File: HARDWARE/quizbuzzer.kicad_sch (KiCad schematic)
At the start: 27 parts, among them J1 Controls, J10 Reciver 5, J11 Reciver 6, J12 Reciver 7, J13 Reciver 8, J14 Reciver 10, J2 MP3out, J25 Conn_02x12_Odd_Even, J26 I2C, J3 I2C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

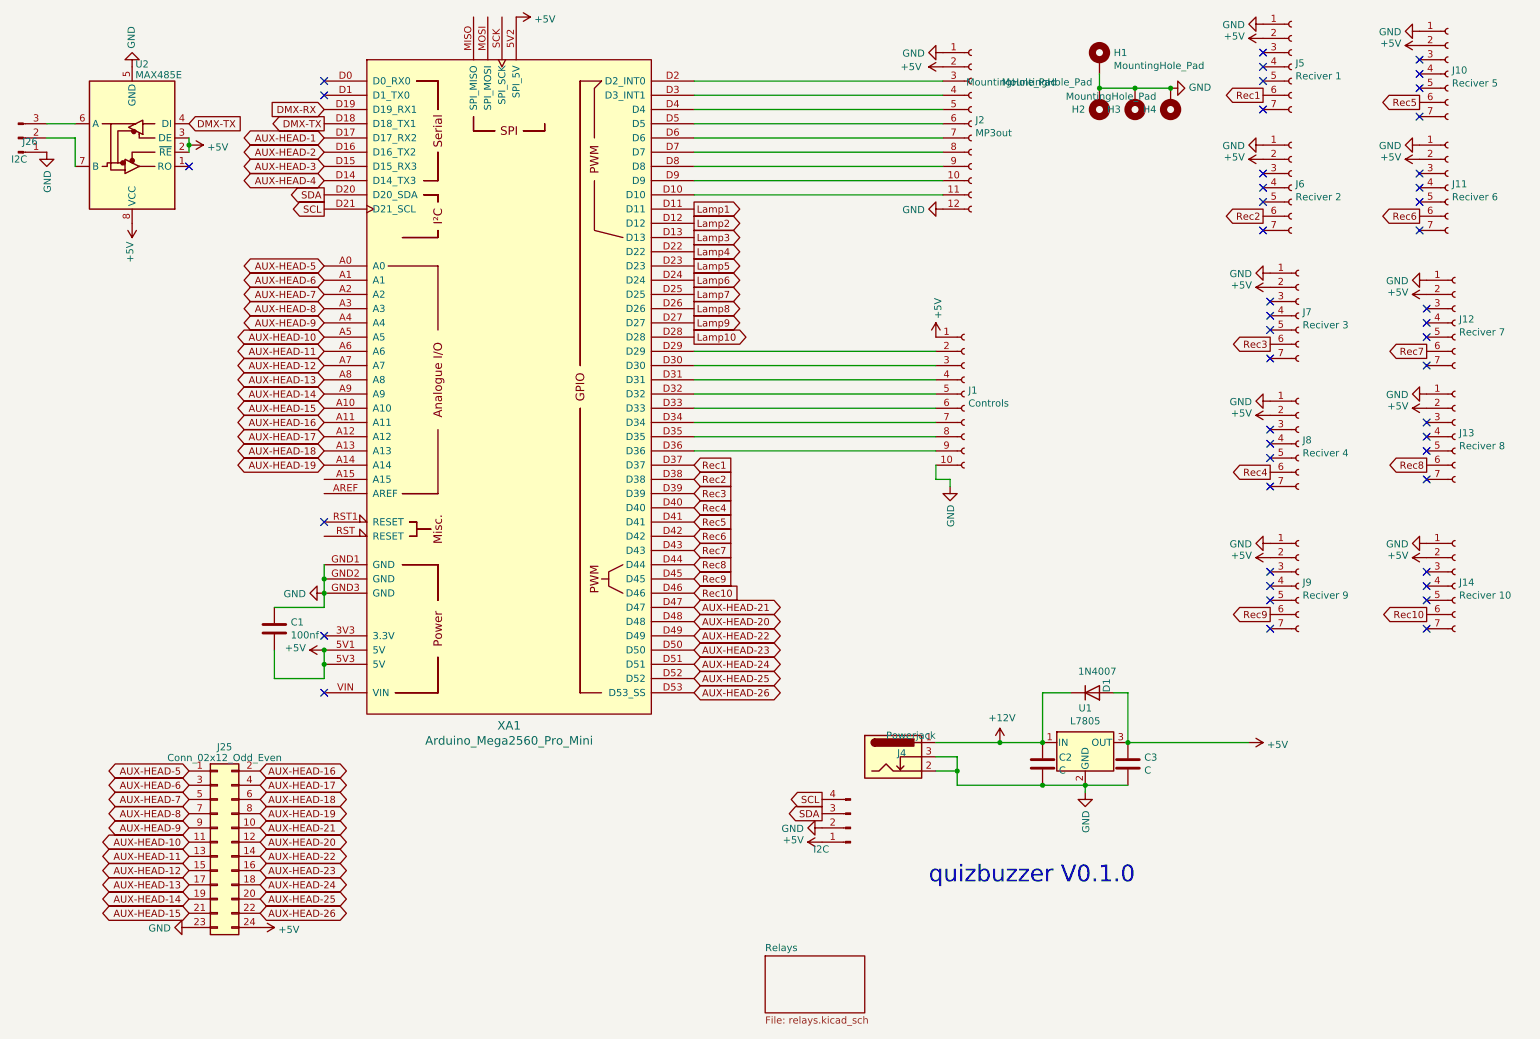
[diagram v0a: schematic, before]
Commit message: Updated schematic for portB, updated code with new variables, stuck at seetting pin mode in loop.
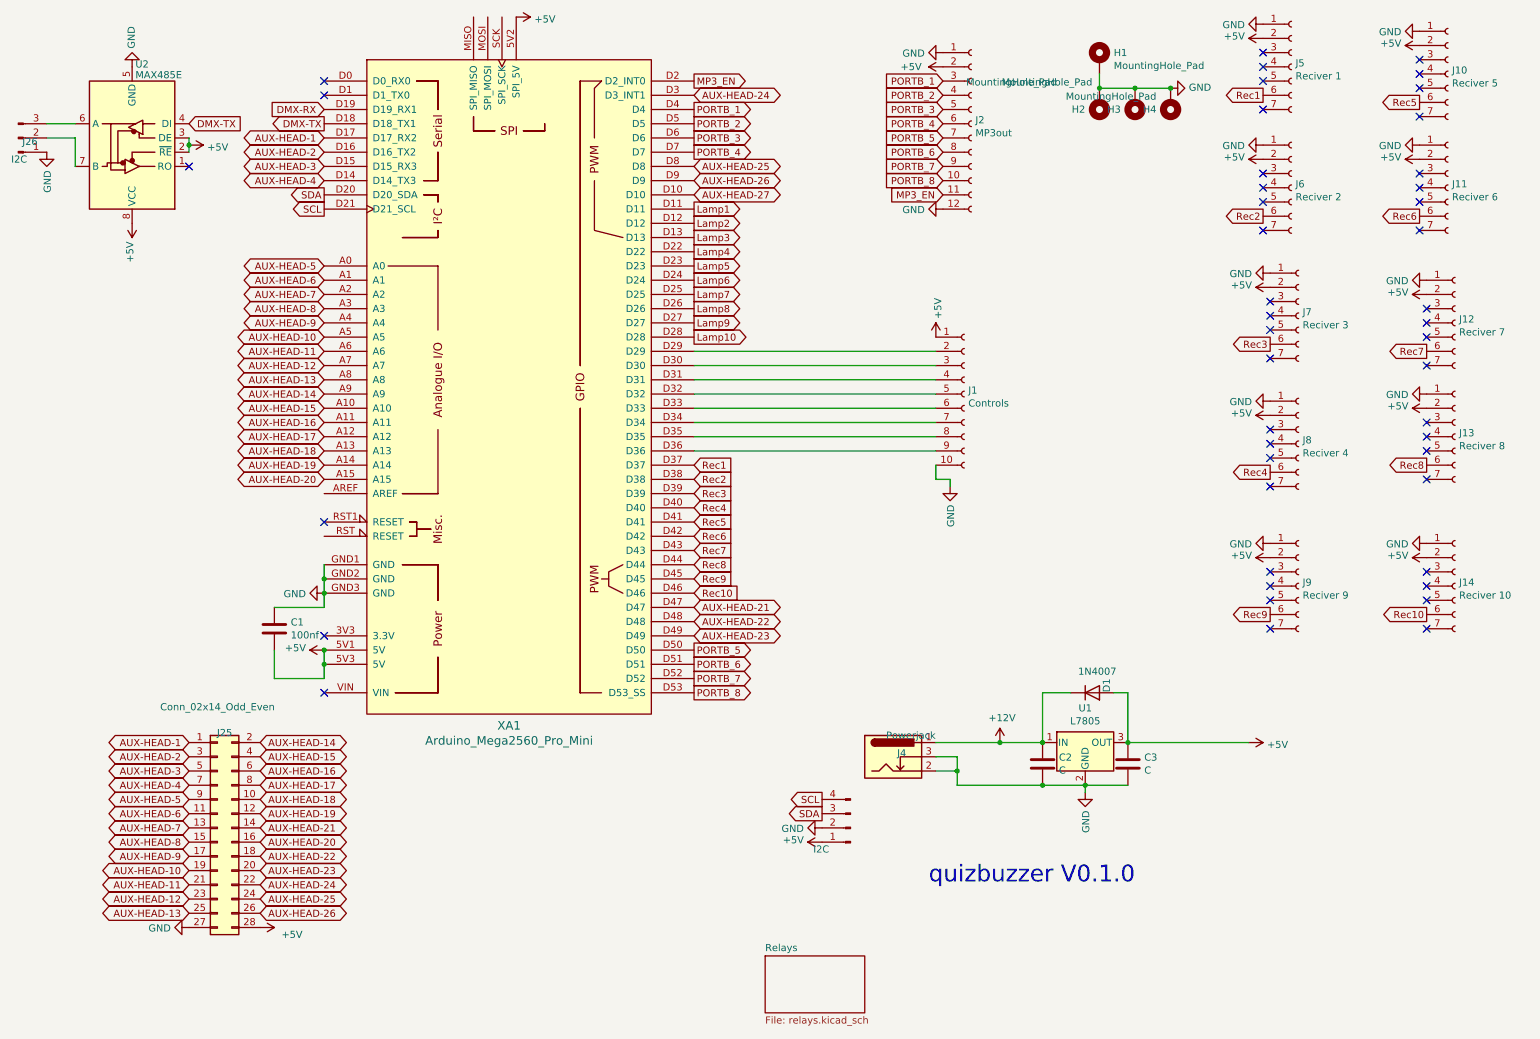
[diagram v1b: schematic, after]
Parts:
- J25: value Conn_02x12_Odd_Even -> Conn_02x14_Odd_Even; footprint Connector_PinHeader_2.54mm:PinHeader_2x12_P2.54mm_Vertical -> Connector_PinHeader_2.54mm:PinHeader_2x14_P2.54mm_Vertical; symbol Connector_Generic:Conn_02x12_Odd_Even -> Connector_Generic:Conn_02x14_Odd_Even
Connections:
- net +5V: now also J25.28 (Pin_28); no longer J25.24 (Pin_24)
- net AUX-HEAD-1: now also J25.1 (Pin_1)
- net AUX-HEAD-10: now also J25.19 (Pin_19); no longer J25.11 (Pin_11)
- net AUX-HEAD-11: now also J25.21 (Pin_21); no longer J25.13 (Pin_13)
- net AUX-HEAD-12: now also J25.23 (Pin_23); no longer J25.15 (Pin_15)
- net AUX-HEAD-13: now also J25.25 (Pin_25); no longer J25.17 (Pin_17)
- net AUX-HEAD-14: now also J25.2 (Pin_2); no longer J25.19 (Pin_19)
- net AUX-HEAD-15: now also J25.4 (Pin_4); no longer J25.21 (Pin_21)
- net AUX-HEAD-16: now also J25.6 (Pin_6); no longer J25.2 (Pin_2)
- net AUX-HEAD-17: now also J25.8 (Pin_8); no longer J25.4 (Pin_4)
- net AUX-HEAD-18: now also J25.10 (Pin_10); no longer J25.6 (Pin_6)
- net AUX-HEAD-19: now also J25.12 (Pin_12); no longer J25.8 (Pin_8)
- net AUX-HEAD-2: now also J25.3 (Pin_3)
- net AUX-HEAD-20: now also J25.16 (Pin_16), XA1.A15; no longer J25.12 (Pin_12), XA1.D48
- net AUX-HEAD-21: now also J25.14 (Pin_14); no longer J25.10 (Pin_10)
- net AUX-HEAD-22: now also J25.18 (Pin_18), XA1.D48; no longer J25.14 (Pin_14), XA1.D49
- net AUX-HEAD-23: now also J25.20 (Pin_20), XA1.D49; no longer J25.16 (Pin_16), XA1.D50
- net AUX-HEAD-24: now also J25.22 (Pin_22), XA1.D3 (D3_INT1); no longer J25.18 (Pin_18), XA1.D51
- net AUX-HEAD-25: now also J25.24 (Pin_24), XA1.D8; no longer J25.20 (Pin_20), XA1.D52
- net AUX-HEAD-26: now also J25.26 (Pin_26), XA1.D9; no longer J25.22 (Pin_22), XA1.D53 (D53_SS)
- net AUX-HEAD-3: now also J25.5 (Pin_5)
- net AUX-HEAD-4: now also J25.7 (Pin_7)
- net AUX-HEAD-5: now also J25.9 (Pin_9); no longer J25.1 (Pin_1)
- net AUX-HEAD-6: now also J25.11 (Pin_11); no longer J25.3 (Pin_3)
- net AUX-HEAD-7: now also J25.13 (Pin_13); no longer J25.5 (Pin_5)
- net AUX-HEAD-8: now also J25.15 (Pin_15); no longer J25.7 (Pin_7)
- net AUX-HEAD-9: now also J25.17 (Pin_17); no longer J25.9 (Pin_9)
- net GND: now also J25.27 (Pin_27); no longer J25.23 (Pin_23)
- net PORTB_8: now reaches J2.10 (Pin_10)
- net PORTB_8: now also XA1.D53 (D53_SS); no longer XA1.D9
- net AUX-HEAD-27: now reaches XA1.D10
- net AUX-HEAD-27: no longer J2.11 (Pin_11)
- net MP3_EN: now reaches XA1.D2 (D2_INT0)
- net MP3_EN: now also J2.11 (Pin_11); no longer J2.3 (Pin_3)
- net PORTB_2: now reaches J2.4 (Pin_4)
- net PORTB_2: now also XA1.D5; no longer XA1.D3 (D3_INT1)
- net PORTB_1: now reaches XA1.D4
- net PORTB_1: now also J2.3 (Pin_3); no longer J2.5 (Pin_5)
- net PORTB_4: now reaches J2.6 (Pin_6)
- net PORTB_4: now also XA1.D7; no longer XA1.D5
- net PORTB_3: now reaches XA1.D6
- net PORTB_3: now also J2.5 (Pin_5); no longer J2.7 (Pin_7)
- net PORTB_6: now reaches J2.8 (Pin_8)
- net PORTB_6: now also XA1.D51; no longer XA1.D7
- net PORTB_7: now reaches J2.9 (Pin_9)
- net PORTB_7: now also XA1.D52; no longer XA1.D8
- new net PORTB_5: J2.7 (Pin_7), XA1.D50

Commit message: FIXLAYER
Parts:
- J26: value I2C -> DMX
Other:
- note removed: "quizbuzzer V0.1.0"
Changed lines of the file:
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@@
     (stroke (width 0) (type default))
-  )
-  (text "quizbuzzer V0.1.0" (at 179.07 171.45 0)
-    (effects (font (size 2.9972 2.9972)) (justify left bottom))
   )
   (global_label "Lamp2" (shape output) (at 137.16 53.34 0)
@@
       (effects (font (size 1.27 1.27)) (justify left))
     )
-    (property "Value" "I2C" (at 15.24 41.91 0)
-      (effects (font (size 1.27 1.27)) (justify left))
-    )
+    (property "Value" "DMX" (at 15.24 41.91 0)
+      (effects (font (size 1.27 1.27)) (justify left))
+    )

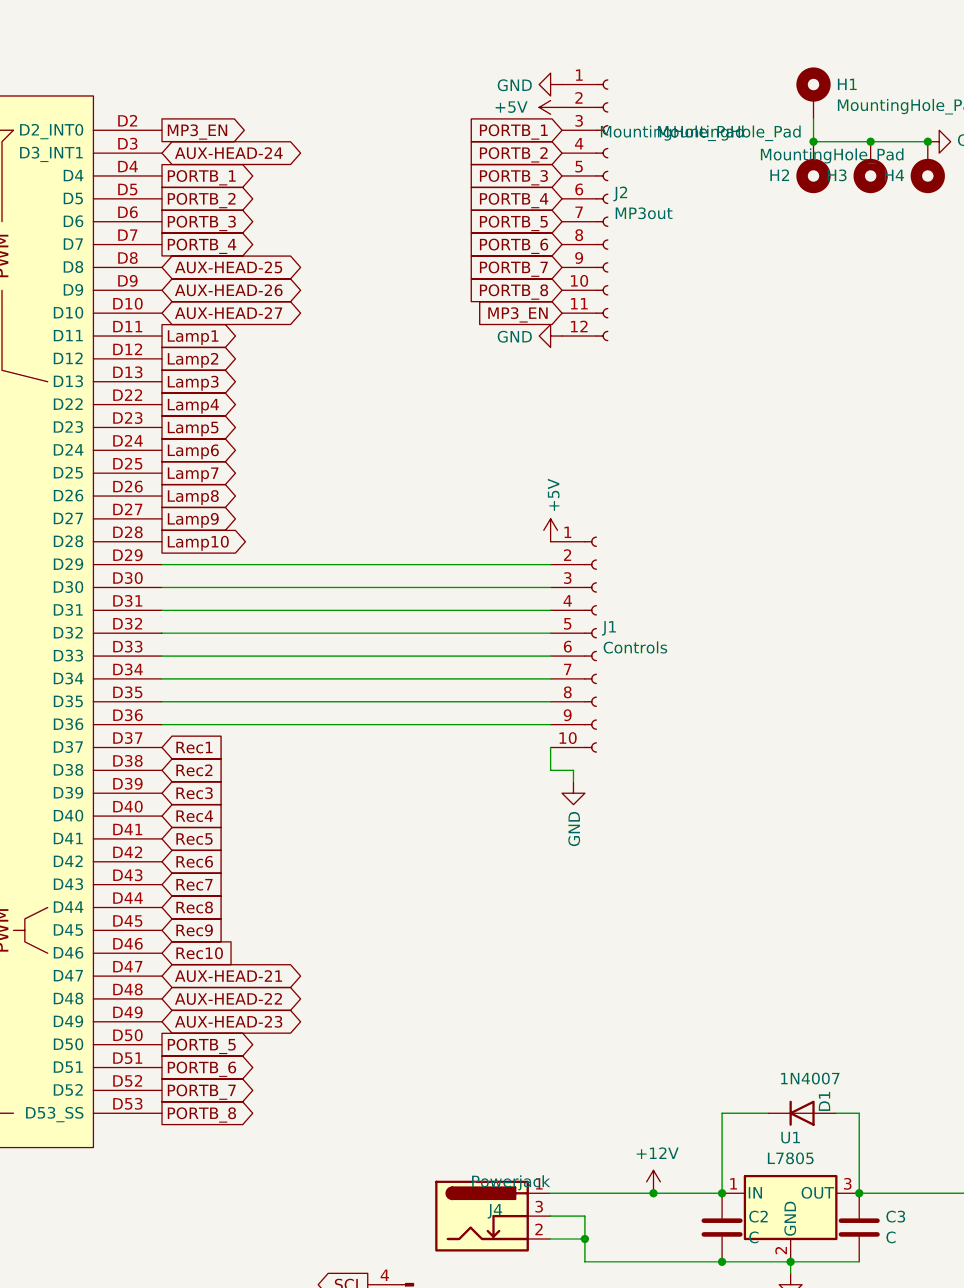
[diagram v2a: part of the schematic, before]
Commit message: Port Sort + 10 to 8 channel
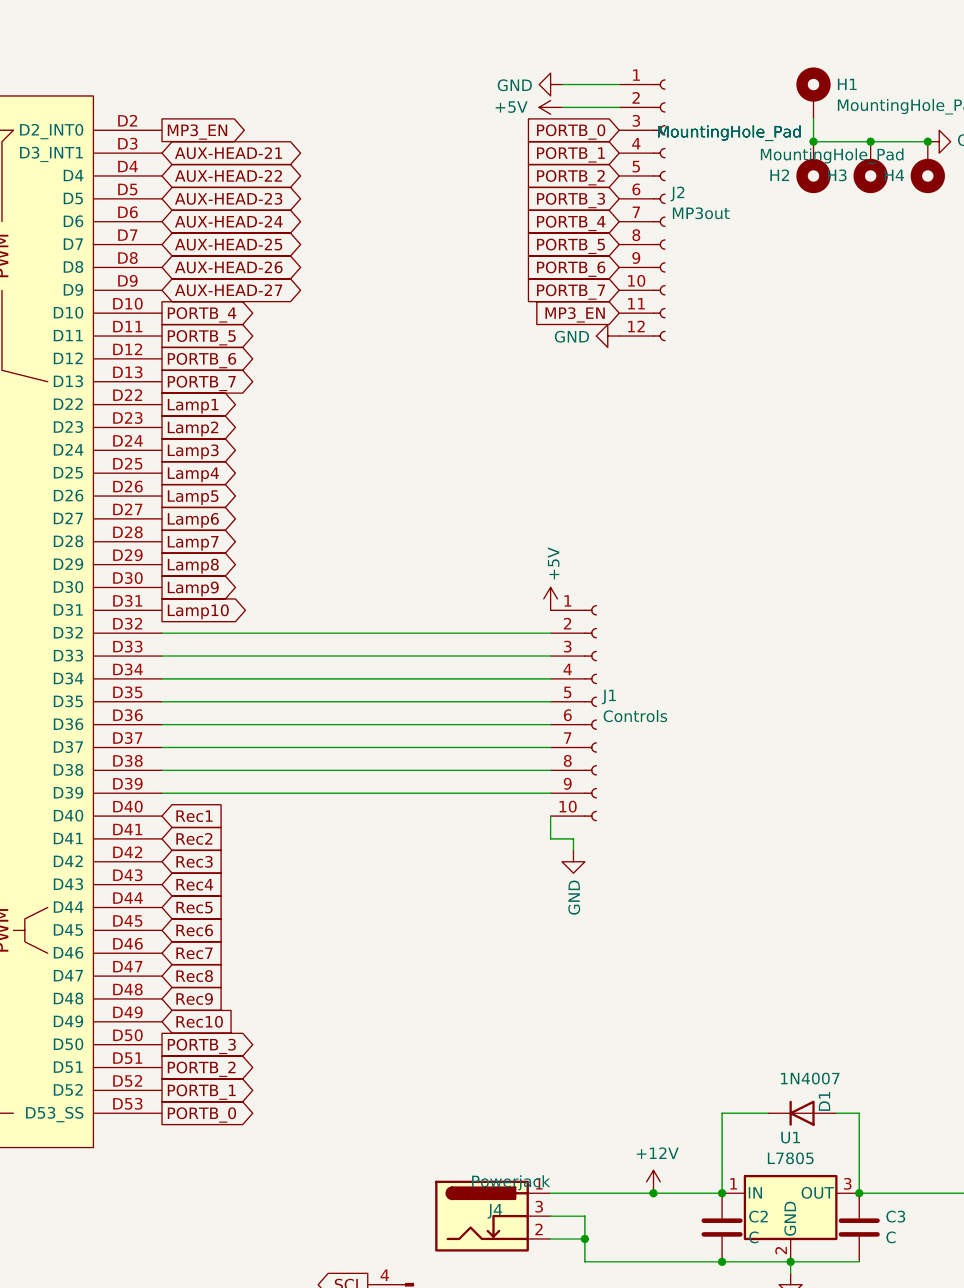
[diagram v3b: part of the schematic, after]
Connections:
- net AUX-HEAD-21: now also XA1.D3 (D3_INT1); no longer XA1.D47
- net AUX-HEAD-22: now also XA1.D4; no longer XA1.D48
- net AUX-HEAD-23: now also XA1.D5; no longer XA1.D49
- net AUX-HEAD-24: now also XA1.D6; no longer XA1.D3 (D3_INT1)
- net AUX-HEAD-25: now also XA1.D7; no longer XA1.D8
- net AUX-HEAD-26: now also XA1.D8; no longer XA1.D9
- net AUX-HEAD-27: now also XA1.D9; no longer XA1.D10
- net Lamp1: now also XA1.D22; no longer XA1.D11
- net Lamp10: now also XA1.D31; no longer XA1.D28
- net Lamp2: now also XA1.D23; no longer XA1.D12
- net Lamp3: now also XA1.D24; no longer XA1.D13
- net Lamp4: now also XA1.D25; no longer XA1.D22
- net Lamp5: now also XA1.D26; no longer XA1.D23
- net Lamp6: now also XA1.D27; no longer XA1.D24
- net Lamp7: now also XA1.D28; no longer XA1.D25
- net Lamp8: now also XA1.D29; no longer XA1.D26
- net Lamp9: now also XA1.D30; no longer XA1.D27
- net PORTB_1: now also J2.4 (Pin_4), XA1.D52; no longer J2.3 (Pin_3), XA1.D4
- net PORTB_2: now also J2.5 (Pin_5), XA1.D51; no longer J2.4 (Pin_4), XA1.D5
- net PORTB_3: now also J2.6 (Pin_6), XA1.D50; no longer J2.5 (Pin_5), XA1.D6
- net PORTB_4: now also J2.7 (Pin_7), XA1.D10; no longer J2.6 (Pin_6), XA1.D7
- net PORTB_5: now also J2.8 (Pin_8), XA1.D11; no longer J2.7 (Pin_7), XA1.D50
- net PORTB_6: now also J2.9 (Pin_9), XA1.D12; no longer J2.8 (Pin_8), XA1.D51
- net PORTB_7: now also J2.10 (Pin_10), XA1.D13; no longer J2.9 (Pin_9), XA1.D52
- net Rec1: now also XA1.D40; no longer XA1.D37
- net Rec10: now also XA1.D49; no longer XA1.D46
- net Rec2: now also XA1.D41; no longer XA1.D38
- net Rec3: now also XA1.D42; no longer XA1.D39
- net Rec4: now also XA1.D43; no longer XA1.D40
- net Rec5: now also XA1.D44; no longer XA1.D41
- net Rec6: now also XA1.D45; no longer XA1.D42
- net Rec7: now also XA1.D46; no longer XA1.D43
- net Rec8: now also XA1.D47; no longer XA1.D44
- net Rec9: now also XA1.D48; no longer XA1.D45
- net at J1.2 (Pin_2): now also XA1.D32; no longer XA1.D29
- net at J1.3 (Pin_3): now also XA1.D33; no longer XA1.D30
- net at J1.4 (Pin_4): now also XA1.D34; no longer XA1.D31
- net at J1.5 (Pin_5): now also XA1.D35; no longer XA1.D32
- net at J1.6 (Pin_6): now also XA1.D36; no longer XA1.D33
- net at J1.7 (Pin_7): now also XA1.D37; no longer XA1.D34
- net at J1.8 (Pin_8): now also XA1.D38; no longer XA1.D35
- net at J1.9 (Pin_9): now also XA1.D39; no longer XA1.D36
- net PORTB_8 renamed PORTB_0
- net PORTB_0: now also J2.3 (Pin_3); no longer J2.10 (Pin_10)
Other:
- moved on the sheet: J1, J2

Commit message: Code sanitisation part 1
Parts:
- removed J14: Reciver 10, Connector_PinSocket_2.54mm:PinSocket_1x07_P2.54mm_Vertical, symbol quizbuzzer-rescue:Conn_01x07_Female-Connector
- removed J9: Reciver 9, Connector_PinSocket_2.54mm:PinSocket_1x07_P2.54mm_Vertical, symbol quizbuzzer-rescue:Conn_01x07_Female-Connector
- J25: value Conn_02x14_Odd_Even -> Conn_02x09_Odd_Even; footprint Connector_PinHeader_2.54mm:PinHeader_2x14_P2.54mm_Vertical -> Connector_PinHeader_2.54mm:PinHeader_2x09_P2.54mm_Vertical; symbol Connector_Generic:Conn_02x14_Odd_Even -> Connector_Generic:Conn_02x09_Odd_Even
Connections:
- net AUX-HEAD-20 is gone; now on net AUX-HEAD-16: J25.16 (Pin_16), XA1.A15
- net Lamp10 is gone; now on an unnamed net: XA1.D31
- net Lamp9 is gone; now on an unnamed net: XA1.D30
- net Rec10 is gone; now on net Rec8: XA1.D49
- net Rec9 is gone; now on net Rec7: XA1.D48
- net +5V: now also J25.18 (Pin_18); no longer J25.28 (Pin_28)
- net AUX-HEAD-1: now also XA1.A0; no longer XA1.D17 (D17_RX2)
- net AUX-HEAD-10: now also J25.4 (Pin_4), XA1.A9; no longer J25.19 (Pin_19), XA1.A5
- net AUX-HEAD-11: now also J25.6 (Pin_6), XA1.A10; no longer J25.21 (Pin_21), XA1.A6
- net AUX-HEAD-12: now also J25.8 (Pin_8), XA1.A11; no longer J25.23 (Pin_23), XA1.A7
- net AUX-HEAD-13: now also J25.10 (Pin_10), XA1.A12; no longer J25.25 (Pin_25), XA1.A8
- net AUX-HEAD-14: now also J25.12 (Pin_12), XA1.A13; no longer J25.2 (Pin_2), XA1.A9
- net AUX-HEAD-15: now also J25.14 (Pin_14), XA1.A14; no longer J25.4 (Pin_4), XA1.A10
- net AUX-HEAD-16: no longer J25.6 (Pin_6), XA1.A11
- net AUX-HEAD-2: now also XA1.A1; no longer XA1.D16 (D16_TX2)
- net AUX-HEAD-3: now also XA1.A2; no longer XA1.D15 (D15_RX3)
- net AUX-HEAD-4: now also XA1.A3; no longer XA1.D14 (D14_TX3)
- net AUX-HEAD-5: now also XA1.A4; no longer XA1.A0
- net AUX-HEAD-6: now also XA1.A5; no longer XA1.A1
- net AUX-HEAD-7: now also XA1.A6; no longer XA1.A2
- net AUX-HEAD-8: now also XA1.A7; no longer XA1.A3
- net AUX-HEAD-9: now also J25.2 (Pin_2), XA1.A8; no longer J25.17 (Pin_17), XA1.A4
- net GND: now also J25.17 (Pin_17); no longer J25.27 (Pin_27)
- net Rec1: now also XA1.D42; no longer XA1.D40
- net Rec2: now also XA1.D43; no longer XA1.D41
- net Rec3: now also XA1.D44; no longer XA1.D42
- net Rec4: now also XA1.D45; no longer XA1.D43
- net Rec5: now also XA1.D46; no longer XA1.D44
- net Rec6: now also XA1.D47; no longer XA1.D45
- net Rec7: no longer XA1.D46
- net Rec8: no longer XA1.D47
- net at J1.2 (Pin_2): no longer XA1.D32
- net at J1.3 (Pin_3): no longer XA1.D33
- net at J1.4 (Pin_4): now also XA1.D32; no longer XA1.D34
- net at J1.5 (Pin_5): now also XA1.D33; no longer XA1.D35
- net at J1.6 (Pin_6): now also XA1.D34; no longer XA1.D36
- net at J1.7 (Pin_7): now also XA1.D35; no longer XA1.D37
- net at J1.8 (Pin_8): now also XA1.D36; no longer XA1.D38
- net at J1.9 (Pin_9): now also XA1.D37; no longer XA1.D39
- removed net AUX-HEAD-17: J25.8 (Pin_8), XA1.A12
- removed net AUX-HEAD-18: J25.10 (Pin_10), XA1.A13
- removed net AUX-HEAD-19: J25.12 (Pin_12), XA1.A14
- net AUX-HEAD-21: no longer names the net of XA1.D3 (D3_INT1)
- net AUX-HEAD-21: no longer J25.14 (Pin_14)
- net AUX-HEAD-22: no longer names the net of XA1.D4
- net AUX-HEAD-22: no longer J25.18 (Pin_18)
- net AUX-HEAD-23: no longer names the net of XA1.D5
- net AUX-HEAD-23: no longer J25.20 (Pin_20)
- net AUX-HEAD-24: no longer names the net of XA1.D6
- net AUX-HEAD-24: no longer J25.22 (Pin_22)
- net AUX-HEAD-25: no longer names the net of XA1.D7
- net AUX-HEAD-25: no longer J25.24 (Pin_24)
- net AUX-HEAD-26: no longer names the net of XA1.D8
- net AUX-HEAD-26: no longer J25.26 (Pin_26)
- net AUX-HEAD-27: no longer names the net of XA1.D9
- no-connect marks 46 -> 38
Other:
- note added: "PORTB"
- note added: "PORTC"
- note added: "PORTF"
- note added: "PORTK"
- note added: "PORTL"
- moved on the sheet: J1
